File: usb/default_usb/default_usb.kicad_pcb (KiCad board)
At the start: 2 copper layers, 4 parts

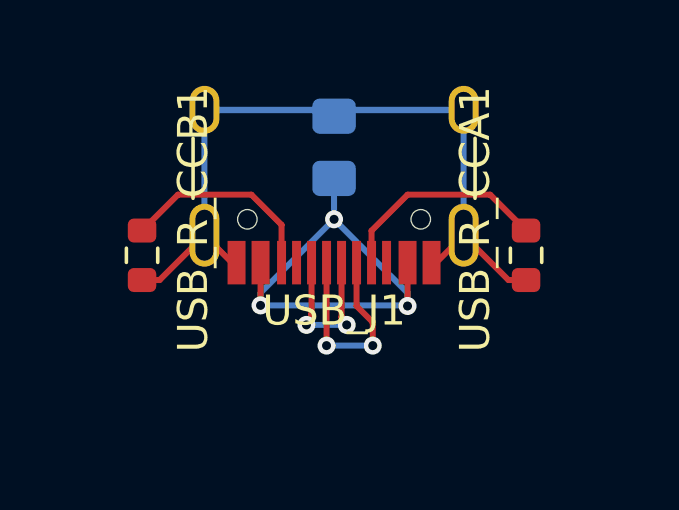
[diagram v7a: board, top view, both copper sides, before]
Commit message: add country yard to power swith
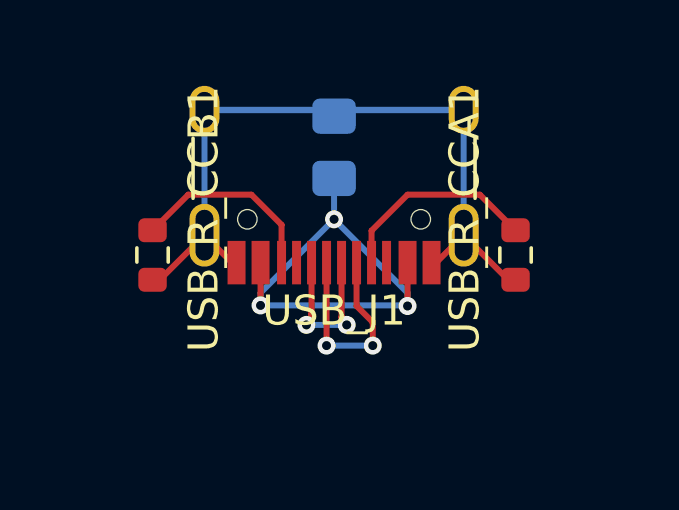
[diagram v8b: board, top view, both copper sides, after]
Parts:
- moved USB_R_CCA1 0.35 mm to (6.05, 3.79)
- moved USB_R_CCB1 0.35 mm to (-6.05, 3.79)
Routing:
- net GND: track 34.6 -> 33.9 mm
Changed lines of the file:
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@@
 	(footprint "ErgoCai.pretty:R_0603_1608Metric"
 		(layer "F.Cu")
-		(at -6.4 3.8 -90)
+		(at -6.05 3.79 -90)
 		(descr "Resistor SMD 0603 (1608 Metric), square (rectangular) end terminal, IPC_7351 nominal, (Body size source: IPC-SM-782 page 72, https://www.pcb-3d.com/wordpress/wp-content/uploads/ipc-sm-782a_amendment_1_and_2.pdf), generated with kicad-footprint-generator")
 		(tags "resistor")
@@
 	(footprint "ErgoCai.pretty:R_0603_1608Metric"
 		(layer "F.Cu")
-		(at 6.4 3.8 -90)
+		(at 6.05 3.79 -90)
 		(descr "Resistor SMD 0603 (1608 Metric), square (rectangular) end terminal, IPC_7351 nominal, (Body size source: IPC-SM-782 page 72, https://www.pcb-3d.com/wordpress/wp-content/uploads/ipc-sm-782a_amendment_1_and_2.pdf), generated with kicad-footprint-generator")
 		(tags "resistor")
@@
 	)
 	(segment
-		(start -6.4 4.625)
-		(end -5.815 4.625)
-		(width 0.2)
-		(layer "F.Cu")
-		(net 2)
-	)
-	(segment
-		(start 4.32 3.13)
-		(end 5.815 4.625)
+		(start -6.05 4.615)
+		(end -5.805 4.615)
 		(width 0.2)
 		(layer "F.Cu")
@@
 	)
 	(segment
-		(start -5.815 4.625)
-		(end -4.32 3.13)
+		(start 6.05 4.615)
+		(end 5.805 4.615)
 		(width 0.2)
 		(layer "F.Cu")
@@
 	)
 	(segment
-		(start 5.815 4.625)
-		(end 6.4 4.625)
+		(start -5.805 4.615)
+		(end -4.32 3.13)
 		(width 0.2)
 		(layer "F.Cu")
@@
 	(segment
 		(start 3.405 4.045)
+		(end 4.32 3.13)
+		(width 0.2)
+		(layer "F.Cu")
+		(net 2)
+	)
+	(segment
+		(start 5.805 4.615)
 		(end 4.32 3.13)
 		(width 0.2)
@@
 	)
 	(segment
-		(start 5.204 1.779)
+		(start 4.86 1.779)
 		(end 2.451 1.779)
 		(width 0.2)
@@
 	)
 	(segment
-		(start 6.4 2.975)
-		(end 5.204 1.779)
+		(start 6.05 2.965)
+		(end 6.046 2.965)
+		(width 0.2)
+		(layer "F.Cu")
+		(net 4)
+	)
+	(segment
+		(start 6.046 2.965)
+		(end 4.86 1.779)
 		(width 0.2)
 		(layer "F.Cu")
@@
 	)
 	(segment
-		(start -6.4 2.975)
-		(end -5.204 1.779)
+		(start -6.05 2.965)
+		(end -6.046 2.965)
 		(width 0.2)
 		(layer "F.Cu")
@@
 	)
 	(segment
-		(start -5.204 1.779)
+		(start -4.86 1.779)
 		(end -2.754992 1.779)
 		(width 0.2)
 		(layer "F.Cu")
+		(net 6)
+	)
+	(segment
+		(start -6.046 2.965)
+		(end -4.86 1.779)
+		(width 0.2)
+		(layer "F.Cu")
